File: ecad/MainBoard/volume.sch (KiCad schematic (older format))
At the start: 10 parts, among them Q2 2N4401BU

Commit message: Update BOM and SPIRCE SIM
Add netlist to calculate power dissipation through each resistor
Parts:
- C10: MPN (none) -> CL03A104MP3NNNC
- C11: MPN (none) -> 0603ZD106KAT2A
- C8: Digi-Key_PN (none) -> 1276-1943-2-ND; MPN (none) -> 1276-1943-2-ND
- Q2: MPN 2N4401BU -> 2N4401-ND
- R12: Digi-Key_PN (none) -> 2019-RN73R2ATTD5053F100TR-ND; MPN (none) -> RN73R2ATTD5053F100
- R13, R14: Digi-Key_PN (none) -> RG2012N-474-W-T1; MPN (none) -> RG20N470KWTR-ND
- R15: Digi-Key_PN (none) -> 311-100DGTR-ND; MPN (none) -> RC0100FR-07100RL
- R18: Digi-Key_PN (none) -> A130048TR-ND; MPN (none) -> CRGCQ0402J1K0
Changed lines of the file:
@@
 F 2 "Capacitor_SMD:C_0805_2012Metric_Pad1.18x1.45mm_HandSolder" H 888 650 50  0001 C CNN
 F 3 "~" H 850 800 50  0001 C CNN
+F 4 "1276-1943-2-ND" H 850 800 50  0001 C CNN "Digi-Key_PN"
+F 5 "1276-1943-2-ND" H 850 800 50  0001 C CNN "MPN"
 	1    850  800
 	0    1    1    0
@@
 F 2 "Resistor_SMD:R_0805_2012Metric_Pad1.20x1.40mm_HandSolder" V 1130 800 50  0001 C CNN
 F 3 "~" H 1200 800 50  0001 C CNN
+F 4 "A130048TR-ND" H 1200 800 50  0001 C CNN "Digi-Key_PN"
+F 5 "CRGCQ0402J1K0" H 1200 800 50  0001 C CNN "MPN"
 	1    1200 800
 	0    1    1    0
@@
 F 1 "0u1" V 1739 950 50  0000 C CNN
 F 2 "Capacitor_SMD:C_0805_2012Metric_Pad1.18x1.45mm_HandSolder" H 1938 800 50  0001 C CNN
-F 3 "~" H 1900 950 50  0001 C CNN
+F 3 "http://www.samsungsem.com/kr/support/product-search/mlcc/CL03A104MP3NNNC.jsp" H 1900 950 50  0001 C CNN
 F 4 "C" H 1900 950 50  0001 C CNN "Spice_Primitive"
 F 5 "0.1u" H 1900 950 50  0001 C CNN "Spice_Model"
 F 6 "Y" H 1900 950 50  0001 C CNN "Spice_Netlist_Enabled"
+F 7 "CL03A104MP3NNNC" H 1900 950 50  0001 C CNN "MPN"
 	1    1900 950
 	0    1    1    0
@@
 F 2 "Resistor_SMD:R_0805_2012Metric_Pad1.20x1.40mm_HandSolder" V 2030 1400 50  0001 C CNN
 F 3 "~" H 2100 1400 50  0001 C CNN
+F 4 "2019-RN73R2ATTD5053F100TR-ND" H 2100 1400 50  0001 C CNN "Digi-Key_PN"
+F 5 "RN73R2ATTD5053F100" H 2100 1400 50  0001 C CNN "MPN"
 	1    2100 1400
 	1    0    0    -1
@@
 F 2 "Resistor_SMD:R_0805_2012Metric_Pad1.20x1.40mm_HandSolder" V 2380 1400 50  0001 C CNN
 F 3 "~" H 2450 1400 50  0001 C CNN
+F 4 "RG2012N-474-W-T1" H 2450 1400 50  0001 C CNN "Digi-Key_PN"
+F 5 "RG20N470KWTR-ND" H 2450 1400 50  0001 C CNN "MPN"
 	1    2450 1400
 	1    0    0    -1
@@
 F 1 "100" V 3034 1200 50  0000 C CNN
 F 2 "Resistor_SMD:R_0805_2012Metric_Pad1.20x1.40mm_HandSolder" V 3080 1200 50  0001 C CNN
-F 3 "~" H 3150 1200 50  0001 C CNN
+F 3 "https://www.yageo.com/upload/media/product/productsearch/datasheet/rchip/PYu-RC_Group_51_RoHS_L_11.pdf" H 3150 1200 50  0001 C CNN
+F 4 "311-100DGTR-ND" H 3150 1200 50  0001 C CNN "Digi-Key_PN"
+F 5 "RC0100FR-07100RL" H 3150 1200 50  0001 C CNN "MPN"
 	1    3150 1200
 	0    1    1    0
@@
 F 1 "10u" V 3664 1200 50  0000 C CNN
 F 2 "Capacitor_SMD:C_0805_2012Metric_Pad1.18x1.45mm_HandSolder" H 3538 1050 50  0001 C CNN
-F 3 "~" H 3500 1200 50  0001 C CNN
+F 3 "https://datasheets.avx.com/cx5r.pdf" H 3500 1200 50  0001 C CNN
+F 4 "0603ZD106KAT2A" H 3500 1200 50  0001 C CNN "MPN"
 	1    3500 1200
 	0    -1   -1   0
@@
 F 2 "Resistor_SMD:R_0805_2012Metric_Pad1.20x1.40mm_HandSolder" V 3630 1400 50  0001 C CNN
 F 3 "~" H 3700 1400 50  0001 C CNN
+F 4 "RG2012N-474-W-T1" H 3700 1400 50  0001 C CNN "Digi-Key_PN"
+F 5 "RG20N470KWTR-ND" H 3700 1400 50  0001 C CNN "MPN"
 	1    3700 1400
 	1    0    0    -1
@@
 F 3 "https://www.onsemi.com/pub/Collateral/MMBT4401-D.PDF" H 2550 1250 60  0001 L CNN
 F 4 "2N4401-ND" H 2550 1350 60  0001 L CNN "Digi-Key_PN"
-F 5 "2N4401BU" H 2550 1450 60  0001 L CNN "MPN"
+F 5 "2N4401-ND" H 2550 1450 60  0001 L CNN "MPN"
 F 6 "Discrete Semiconductor Products" H 2550 1550 60  0001 L CNN "Category"
 F 7 "Transistors - Bipolar (BJT) - Single" H 2550 1650 60  0001 L CNN "Family"

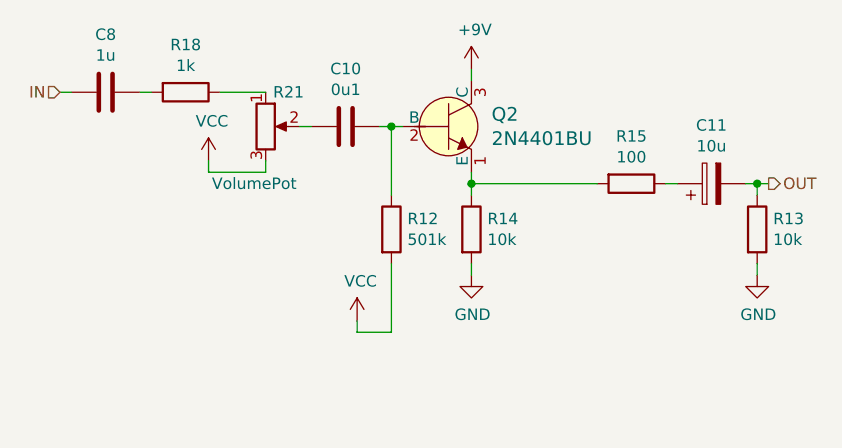
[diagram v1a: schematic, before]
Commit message: Corrections + SPICE Model Finally fixed :)
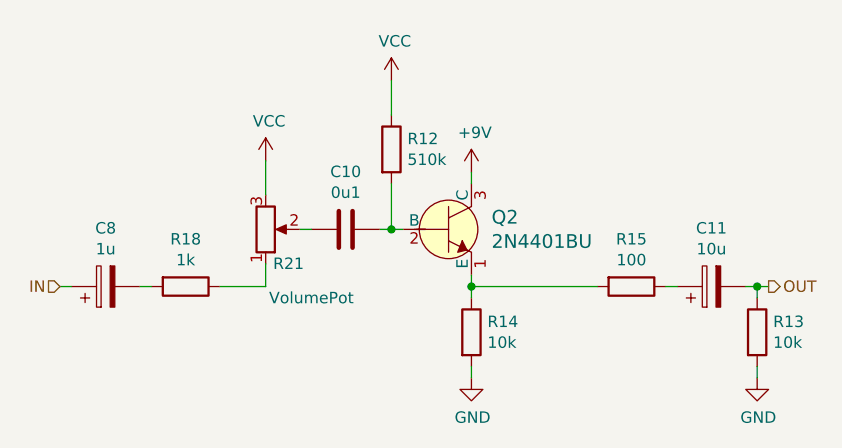
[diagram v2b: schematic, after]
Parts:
- removed C8: 1u, Capacitor_SMD:C_0805_2012Metric_Pad1.18x1.45mm_HandSolder, symbol Device:C
- added C8: 1u, Capacitor_SMD:C_0805_2012Metric_Pad1.18x1.45mm_HandSolder, symbol Device:CP
- Q2: Spice_Lib_File /home/john/dox/cad/screaming-panda/ecad/lib/spice_models/2N4401.lib -> /home/john/dox/cad/screaming-panda/ecad/lib/spice_models/2N4401BU.lib; Spice_Node_Sequence (none) -> 3 2 1
- R12: value 501k -> 510k
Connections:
- net IN: now also C8.1
- net VCC: now also R12.1; no longer R12.2
- net at R18.2: now also C8.2
- net at C10.1, Q2.2 (B): now also R12.2; no longer R12.1
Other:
- moved on the sheet: C10, C11, Q2, R12, R13, R14, R15, R18, R21

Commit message: Clean up ecad
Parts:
- C10: footprint Capacitor_SMD:C_0805_2012Metric_Pad1.18x1.45mm_HandSolder -> Capacitor_SMD:C_0201_0603Metric_Pad0.64x0.40mm_HandSolder; Digi-Key_PN (none) -> 1276-1321-6-ND
- C11: footprint Capacitor_SMD:C_0805_2012Metric_Pad1.18x1.45mm_HandSolder -> Capacitor_SMD:C_0603_1608Metric_Pad1.08x0.95mm_HandSolder; Digi-Key_PN (none) -> 478-10766-6-ND
- C8: footprint Capacitor_SMD:C_0805_2012Metric_Pad1.18x1.45mm_HandSolder -> Capacitor_SMD:C_0603_1608Metric_Pad1.08x0.95mm_HandSolder; Digi-Key_PN (none) -> 0603ZD106KAT2A
- R15: footprint Resistor_SMD:R_0805_2012Metric_Pad1.20x1.40mm_HandSolder -> Resistor_SMD:R_1218_3246Metric_Pad1.22x4.75mm_HandSolder; Digi-Key_PN 311-100DGTR-ND -> 541-100ANDKR-ND; MPN RC0100FR-07100RL -> CRCW1218100RFKEKHP
- R18: footprint Resistor_SMD:R_0805_2012Metric_Pad1.20x1.40mm_HandSolder -> Resistor_SMD:R_0402_1005Metric_Pad0.72x0.64mm_HandSolder
- R21: value VolumePot -> 20ka; Category (none) -> Volume Pot; Digi-Key_PN (none) -> 75160-195-08LF; Spice_Lib_File ../lib/spice_models/pot.lib -> ../lib/spice_models/pots.lib
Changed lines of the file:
@@
 encoding utf-8
 Sheet 4 5
-Title "Effects Board"
-Date "2021-01-17"
-Rev "1.0"
-Comp "Panda Pals"
-Comment1 "John McAvoy"
+Title "Screaming Panda Guitar Pedal"
+Date "2021-08-08"
+Rev "1v0"
+Comp "John McAvoy"
+Comment1 ""
 Comment2 ""
 Comment3 ""
@@
 AR Path="/60332464" Ref="R?"  Part="1"
 AR Path="/6030769F/60332464" Ref="R18"  Part="1"
-F 0 "R18" V 993 1650 50  0000 C CNN
-F 1 "1k" V 1084 1650 50  0000 C CNN
-F 2 "Resistor_SMD:R_0805_2012Metric_Pad1.20x1.40mm_HandSolder" V 1130 1650 50  0001 C CNN
-F 3 "~" H 1200 1650 50  0001 C CNN
+F 0 "R18" V 1100 1650 50  0000 C CNN
+F 1 "1k" V 1200 1650 50  0000 C CNN
+F 2 "Resistor_SMD:R_0402_1005Metric_Pad0.72x0.64mm_HandSolder" V 1130 1650 50  0001 C CNN
+F 3 "https://www.te.com/commerce/DocumentDelivery/DDEController?Action=srchrtrv&DocNm=1773204-3&DocType=DS&DocLang=English" H 1200 1650 50  0001 C CNN
 F 4 "A130048TR-ND" H 1200 1650 50  0001 C CNN "Digi-Key_PN"
 F 5 "CRGCQ0402J1K0" H 1200 1650 50  0001 C CNN "MPN"
@@
 F 0 "C10" V 1648 1400 50  0000 C CNN
 F 1 "0u1" V 1739 1400 50  0000 C CNN
-F 2 "Capacitor_SMD:C_0805_2012Metric_Pad1.18x1.45mm_HandSolder" H 1938 1250 50  0001 C CNN
+F 2 "Capacitor_SMD:C_0201_0603Metric_Pad0.64x0.40mm_HandSolder" H 1938 1250 50  0001 C CNN
 F 3 "http://www.samsungsem.com/kr/support/product-search/mlcc/CL03A104MP3NNNC.jsp" H 1900 1400 50  0001 C CNN
 F 4 "C" H 1900 1400 50  0001 C CNN "Spice_Primitive"
@@
 F 6 "Y" H 1900 1400 50  0001 C CNN "Spice_Netlist_Enabled"
 F 7 "CL03A104MP3NNNC" H 1900 1400 50  0001 C CNN "MPN"
+F 8 "1276-1321-6-ND" H 1900 1400 50  0001 C CNN "Digi-Key_PN"
 	1    1900 1400
 	0    1    1    0
@@
 AR Path="/6030769F/60332476" Ref="R12"  Part="1"
 F 0 "R12" H 2170 1096 50  0000 L CNN
-F 1 "510k" H 2170 1005 50  0000 L CNN
+F 1 "510k" V 2100 950 50  0000 L CNN
 F 2 "Resistor_SMD:R_0805_2012Metric_Pad1.20x1.40mm_HandSolder" V 2030 1050 50  0001 C CNN
-F 3 "~" H 2100 1050 50  0001 C CNN
+F 3 "https://media.digikey.com/pdf/Data%20Sheets/KOA%20Speer/RN73R_Type_DS.pdf" H 2100 1050 50  0001 C CNN
 F 4 "2019-RN73R2ATTD5053F100TR-ND" H 2100 1050 50  0001 C CNN "Digi-Key_PN"
 F 5 "RN73R2ATTD5053F100" H 2100 1050 50  0001 C CNN "MPN"
@@
 AR Path="/6030769F/603324B1" Ref="R14"  Part="1"
 F 0 "R14" H 2520 1896 50  0000 L CNN
-F 1 "10k" H 2520 1805 50  0000 L CNN
+F 1 "10k" V 2450 1750 50  0000 L CNN
 F 2 "Resistor_SMD:R_0805_2012Metric_Pad1.20x1.40mm_HandSolder" V 2380 1850 50  0001 C CNN
-F 3 "~" H 2450 1850 50  0001 C CNN
+F 3 "https://www.susumu.co.jp/common/pdf/n_catalog_partition01_en.pdf" H 2450 1850 50  0001 C CNN
 F 4 "RG2012N-474-W-T1" H 2450 1850 50  0001 C CNN "Digi-Key_PN"
 F 5 "RG20N470KWTR-ND" H 2450 1850 50  0001 C CNN "MPN"
@@
 AR Path="/603324BA" Ref="R?"  Part="1"
 AR Path="/6030769F/603324BA" Ref="R15"  Part="1"
-F 0 "R15" V 2943 1650 50  0000 C CNN
-F 1 "100" V 3034 1650 50  0000 C CNN
-F 2 "Resistor_SMD:R_0805_2012Metric_Pad1.20x1.40mm_HandSolder" V 3080 1650 50  0001 C CNN
-F 3 "https://www.yageo.com/upload/media/product/productsearch/datasheet/rchip/PYu-RC_Group_51_RoHS_L_11.pdf" H 3150 1650 50  0001 C CNN
-F 4 "311-100DGTR-ND" H 3150 1650 50  0001 C CNN "Digi-Key_PN"
-F 5 "RC0100FR-07100RL" H 3150 1650 50  0001 C CNN "MPN"
+F 0 "R15" V 3050 1650 50  0000 C CNN
+F 1 "100" V 3150 1650 50  0000 C CNN
+F 2 "Resistor_SMD:R_1218_3246Metric_Pad1.22x4.75mm_HandSolder" V 3080 1650 50  0001 C CNN
+F 3 "https://www.vishay.com/docs/20043/crcwhpe3.pdf" H 3150 1650 50  0001 C CNN
+F 4 "541-100ANDKR-ND" H 3150 1650 50  0001 C CNN "Digi-Key_PN"
+F 5 "CRCW1218100RFKEKHP" H 3150 1650 50  0001 C CNN "MPN"
 	1    3150 1650
 	0    1    1    0
@@
 F 0 "C11" V 3755 1650 50  0000 C CNN
 F 1 "10u" V 3664 1650 50  0000 C CNN
-F 2 "Capacitor_SMD:C_0805_2012Metric_Pad1.18x1.45mm_HandSolder" H 3538 1500 50  0001 C CNN
+F 2 "Capacitor_SMD:C_0603_1608Metric_Pad1.08x0.95mm_HandSolder" H 3538 1500 50  0001 C CNN
 F 3 "https://datasheets.avx.com/cx5r.pdf" H 3500 1650 50  0001 C CNN
 F 4 "0603ZD106KAT2A" H 3500 1650 50  0001 C CNN "MPN"
+F 5 "478-10766-6-ND" H 3500 1650 50  0001 C CNN "Digi-Key_PN"
 	1    3500 1650
 	0    -1   -1   0
@@
 AR Path="/6030769F/603324C6" Ref="R13"  Part="1"
 F 0 "R13" H 3770 1896 50  0000 L CNN
-F 1 "10k" H 3770 1805 50  0000 L CNN
+F 1 "10k" V 3700 1775 50  0000 L CNN
 F 2 "Resistor_SMD:R_0805_2012Metric_Pad1.20x1.40mm_HandSolder" V 3630 1850 50  0001 C CNN
-F 3 "~" H 3700 1850 50  0001 C CNN
+F 3 "https://www.susumu.co.jp/common/pdf/n_catalog_partition01_en.pdf" H 3700 1850 50  0001 C CNN
 F 4 "RG2012N-474-W-T1" H 3700 1850 50  0001 C CNN "Digi-Key_PN"
 F 5 "RG20N470KWTR-ND" H 3700 1850 50  0001 C CNN "MPN"
@@
 F 0 "C8" V 1105 1650 50  0000 C CNN
 F 1 "1u" V 1014 1650 50  0000 C CNN
-F 2 "Capacitor_SMD:C_0805_2012Metric_Pad1.18x1.45mm_HandSolder" H 888 1500 50  0001 C CNN
+F 2 "Capacitor_SMD:C_0603_1608Metric_Pad1.08x0.95mm_HandSolder" H 888 1500 50  0001 C CNN
 F 3 "https://datasheets.avx.com/cx5r.pdf" H 850 1650 50  0001 C CNN
 F 4 "0603ZD106KAT2A" H 850 1650 50  0001 C CNN "MPN"
+F 5 "0603ZD106KAT2A" H 850 1650 50  0001 C CNN "Digi-Key_PN"
 	1    850  1650
 	0    -1   -1   0
@@
 P 1550 1400
 F 0 "R21" H 1650 1550 50  0000 C CNN
-F 1 "VolumePot" H 1750 1700 50  0000 C CNN
+F 1 "20ka" V 1550 1400 50  0000 C CNN
 F 2 "Connector_PinHeader_2.54mm:PinHeader_1x03_P2.54mm_Vertical" H 1550 1400 50  0001 C CNN
-F 3 "~" H 1550 1400 50  0001 C CNN
+F 3 "https://www.bourns.com/docs/Product-Datasheets/PTV09.pdf" H 1550 1400 50  0001 C CNN
 F 4 "X" H 1550 1400 50  0001 C CNN "Spice_Primitive"
 F 5 "POTVolume" H 1550 1400 50  0001 C CNN "Spice_Model"
 F 6 "Y" H 1550 1400 50  0001 C CNN "Spice_Netlist_Enabled"
-F 7 "../lib/spice_models/pot.lib" H 1550 1400 50  0001 C CNN "Spice_Lib_File"
+F 7 "../lib/spice_models/pots.lib" H 1550 1400 50  0001 C CNN "Spice_Lib_File"
+F 8 "Volume Pot" H 1800 1650 50  0000 C CNN "Category"
+F 9 "75160-195-08LF" H 1550 1400 50  0001 C CNN "Digi-Key_PN"
+F 10 "" H 1550 1400 50  0001 C CNN "MPN"
 	1    1550 1400
 	1    0    0    1

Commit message: Update ecad BOM
Change transistor to 2N4424
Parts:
- C10: value 0u1 -> 100n; footprint Capacitor_SMD:C_0201_0603Metric_Pad0.64x0.40mm_HandSolder -> Capacitor_SMD:C_0805_2012Metric_Pad1.18x1.45mm_HandSolder; MPN CL03A104MP3NNNC -> C0805C104K3RACTU
- C11: footprint Capacitor_SMD:C_0603_1608Metric_Pad1.08x0.95mm_HandSolder -> Capacitor_SMD:C_0805_2012Metric_Pad1.18x1.45mm_HandSolder; MPN 0603ZD106KAT2A -> C0805C106K8PACTU
- C8: footprint Capacitor_SMD:C_0603_1608Metric_Pad1.08x0.95mm_HandSolder -> Capacitor_SMD:C_0805_2012Metric_Pad1.18x1.45mm_HandSolder; MPN 0603ZD106KAT2A -> C0805C105K4RACTU
- Q2: value 2N4401BU -> 2N4424; MPN 2N4401-ND -> 2N4424; Spice_Lib_File /home/john/dox/cad/screaming-panda/ecad/lib/spice_models/2N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 -> ../lib/spice_models/2N4424.lib; Spice_Model 2N4401 -> 2N4424
- R12: MPN RN73R2ATTD5053F100 -> ERJ-6ENF5103V
- R13, R14: MPN RG20N470KWTR-ND -> ERJ-6GEYJ103V
- R15: footprint Resistor_SMD:R_1218_3246Metric_Pad1.22x4.75mm_HandSolder -> Resistor_SMD:R_0805_2012Metric_Pad1.20x1.40mm_HandSolder; MPN CRCW1218100RFKEKHP -> ERJ-6GEYJ101V
- R18: footprint Resistor_SMD:R_0402_1005Metric_Pad0.72x0.64mm_HandSolder -> Resistor_SMD:R_0805_2012Metric_Pad1.20x1.40mm_HandSolder; MPN CRGCQ0402J1K0 -> ERA6AEB102V
- R21: footprint Connector_PinHeader_2.54mm:PinHeader_1x03_P2.54mm_Vertical -> DigiKey:PinHeader_1x3_P2.54_Drill1.1mm; MPN (none) -> 0901200160
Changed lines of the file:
@@
 F 0 "R18" V 1100 1650 50  0000 C CNN
 F 1 "1k" V 1200 1650 50  0000 C CNN
-F 2 "Resistor_SMD:R_0402_1005Metric_Pad0.72x0.64mm_HandSolder" V 1130 1650 50  0001 C CNN
-F 3 "https://www.te.com/commerce/DocumentDelivery/DDEController?Action=srchrtrv&DocNm=1773204-3&DocType=DS&DocLang=English" H 1200 1650 50  0001 C CNN
+F 2 "Resistor_SMD:R_0805_2012Metric_Pad1.20x1.40mm_HandSolder" V 1130 1650 50  0001 C CNN
+F 3 "https://datasheet.octopart.com/ERA6AEB102V-Panasonic-datasheet-62287448.pdf" H 1200 1650 50  0001 C CNN
 F 4 "A130048TR-ND" H 1200 1650 50  0001 C CNN "Digi-Key_PN"
-F 5 "CRGCQ0402J1K0" H 1200 1650 50  0001 C CNN "MPN"
+F 5 "ERA6AEB102V" H 1200 1650 50  0001 C CNN "MPN"
 	1    1200 1650
 	0    1    1    0
@@
 AR Path="/6030769F/60332470" Ref="C10"  Part="1"
 F 0 "C10" V 1648 1400 50  0000 C CNN
-F 1 "0u1" V 1739 1400 50  0000 C CNN
-F 2 "Capacitor_SMD:C_0201_0603Metric_Pad0.64x0.40mm_HandSolder" H 1938 1250 50  0001 C CNN
-F 3 "http://www.samsungsem.com/kr/support/product-search/mlcc/CL03A104MP3NNNC.jsp" H 1900 1400 50  0001 C CNN
+F 1 "100n" V 1739 1400 50  0000 C CNN
+F 2 "Capacitor_SMD:C_0805_2012Metric_Pad1.18x1.45mm_HandSolder" H 1938 1250 50  0001 C CNN
+F 3 "https://datasheet.octopart.com/C0805C104K3RAC-TU-Kemet-datasheet-5313890.pdf" H 1900 1400 50  0001 C CNN
 F 4 "C" H 1900 1400 50  0001 C CNN "Spice_Primitive"
 F 5 "0.1u" H 1900 1400 50  0001 C CNN "Spice_Model"
 F 6 "Y" H 1900 1400 50  0001 C CNN "Spice_Netlist_Enabled"
-F 7 "CL03A104MP3NNNC" H 1900 1400 50  0001 C CNN "MPN"
+F 7 "C0805C104K3RACTU" H 1900 1400 50  0001 C CNN "MPN"
 F 8 "1276-1321-6-ND" H 1900 1400 50  0001 C CNN "Digi-Key_PN"
 	1    1900 1400
@@
 F 1 "510k" V 2100 950 50  0000 L CNN
 F 2 "Resistor_SMD:R_0805_2012Metric_Pad1.20x1.40mm_HandSolder" V 2030 1050 50  0001 C CNN
-F 3 "https://media.digikey.com/pdf/Data%20Sheets/KOA%20Speer/RN73R_Type_DS.pdf" H 2100 1050 50  0001 C CNN
+F 3 "https://datasheet.octopart.com/ERJ-6ENF5103V-Panasonic-datasheet-13266541.pdf" H 2100 1050 50  0001 C CNN
 F 4 "2019-RN73R2ATTD5053F100TR-ND" H 2100 1050 50  0001 C CNN "Digi-Key_PN"
-F 5 "RN73R2ATTD5053F100" H 2100 1050 50  0001 C CNN "MPN"
+F 5 "ERJ-6ENF5103V" H 2100 1050 50  0001 C CNN "MPN"
 	1    2100 1050
 	1    0    0    -1
@@
 F 1 "10k" V 2450 1750 50  0000 L CNN
 F 2 "Resistor_SMD:R_0805_2012Metric_Pad1.20x1.40mm_HandSolder" V 2380 1850 50  0001 C CNN
-F 3 "https://www.susumu.co.jp/common/pdf/n_catalog_partition01_en.pdf" H 2450 1850 50  0001 C CNN
+F 3 "https://datasheet.octopart.com/ERJ-6GEYJ103V-Panasonic-datasheet-13266872.pdf" H 2450 1850 50  0001 C CNN
 F 4 "RG2012N-474-W-T1" H 2450 1850 50  0001 C CNN "Digi-Key_PN"
-F 5 "RG20N470KWTR-ND" H 2450 1850 50  0001 C CNN "MPN"
+F 5 "ERJ-6GEYJ103V" H 2450 1850 50  0001 C CNN "MPN"
 	1    2450 1850
 	1    0    0    -1
@@
 F 0 "R15" V 3050 1650 50  0000 C CNN
 F 1 "100" V 3150 1650 50  0000 C CNN
-F 2 "Resistor_SMD:R_1218_3246Metric_Pad1.22x4.75mm_HandSolder" V 3080 1650 50  0001 C CNN
-F 3 "https://www.vishay.com/docs/20043/crcwhpe3.pdf" H 3150 1650 50  0001 C CNN
+F 2 "Resistor_SMD:R_0805_2012Metric_Pad1.20x1.40mm_HandSolder" V 3080 1650 50  0001 C CNN
+F 3 "https://datasheet.octopart.com/ERJ-6GEYJ101V-Panasonic-datasheet-13266872.pdf" H 3150 1650 50  0001 C CNN
 F 4 "541-100ANDKR-ND" H 3150 1650 50  0001 C CNN "Digi-Key_PN"
-F 5 "CRCW1218100RFKEKHP" H 3150 1650 50  0001 C CNN "MPN"
+F 5 "ERJ-6GEYJ101V" H 3150 1650 50  0001 C CNN "MPN"
 	1    3150 1650
 	0    1    1    0
@@
 F 0 "C11" V 3755 1650 50  0000 C CNN
 F 1 "10u" V 3664 1650 50  0000 C CNN
-F 2 "Capacitor_SMD:C_0603_1608Metric_Pad1.08x0.95mm_HandSolder" H 3538 1500 50  0001 C CNN
-F 3 "https://datasheets.avx.com/cx5r.pdf" H 3500 1650 50  0001 C CNN
-F 4 "0603ZD106KAT2A" H 3500 1650 50  0001 C CNN "MPN"
+F 2 "Capacitor_SMD:C_0805_2012Metric_Pad1.18x1.45mm_HandSolder" H 3538 1500 50  0001 C CNN
+F 3 "https://datasheet.octopart.com/C0805C106K8PACTU-KEMET-datasheet-149523945.pdf" H 3500 1650 50  0001 C CNN
+F 4 "C0805C106K8PACTU" H 3500 1650 50  0001 C CNN "MPN"
 F 5 "478-10766-6-ND" H 3500 1650 50  0001 C CNN "Digi-Key_PN"
 	1    3500 1650
@@
 F 1 "10k" V 3700 1775 50  0000 L CNN
 F 2 "Resistor_SMD:R_0805_2012Metric_Pad1.20x1.40mm_HandSolder" V 3630 1850 50  0001 C CNN
-F 3 "https://www.susumu.co.jp/common/pdf/n_catalog_partition01_en.pdf" H 3700 1850 50  0001 C CNN
+F 3 "https://datasheet.octopart.com/ERJ-6GEYJ103V-Panasonic-datasheet-13266872.pdf" H 3700 1850 50  0001 C CNN
 F 4 "RG2012N-474-W-T1" H 3700 1850 50  0001 C CNN "Digi-Key_PN"
-F 5 "RG20N470KWTR-ND" H 3700 1850 50  0001 C CNN "MPN"
+F 5 "ERJ-6GEYJ103V" H 3700 1850 50  0001 C CNN "MPN"
 	1    3700 1850
 	1    0    0    -1
@@
 F 0 "C8" V 1105 1650 50  0000 C CNN
 F 1 "1u" V 1014 1650 50  0000 C CNN
-F 2 "Capacitor_SMD:C_0603_1608Metric_Pad1.08x0.95mm_HandSolder" H 888 1500 50  0001 C CNN
-F 3 "https://datasheets.avx.com/cx5r.pdf" H 850 1650 50  0001 C CNN
-F 4 "0603ZD106KAT2A" H 850 1650 50  0001 C CNN "MPN"
+F 2 "Capacitor_SMD:C_0805_2012Metric_Pad1.18x1.45mm_HandSolder" H 888 1500 50  0001 C CNN
+F 3 "https://datasheet.octopart.com/C0805C105K4RACTU-KEMET-datasheet-149523919.pdf" H 850 1650 50  0001 C CNN
+F 4 "C0805C105K4RACTU" H 850 1650 50  0001 C CNN "MPN"
 F 5 "0603ZD106KAT2A" H 850 1650 50  0001 C CNN "Digi-Key_PN"
 	1    850  1650
@@
 AR Path="/6030769F/60332485" Ref="Q2"  Part="1"
 F 0 "Q2" H 2538 1453 60  0000 L CNN
-F 1 "2N4401BU" H 2538 1347 60  0000 L CNN
+F 1 "2N4424" H 2538 1347 60  0000 L CNN
 F 2 "digikey-footprints:TO-92-3" H 2550 1600 60  0001 L CNN
-F 3 "https://www.onsemi.com/pub/Collateral/MMBT4401-D.PDF" H 2550 1700 60  0001 L CNN
+F 3 "" H 2550 1700 60  0001 L CNN
 F 4 "2N4401-ND" H 2550 1800 60  0001 L CNN "Digi-Key_PN"
-F 5 "2N4401-ND" H 2550 1900 60  0001 L CNN "MPN"
+F 5 "2N4424" H 2550 1900 60  0001 L CNN "MPN"
 F 6 "Discrete Semiconductor Products" H 2550 2000 60  0001 L CNN "Category"
 F 7 "Transistors - Bipolar (BJT) - Single" H 2550 2100 60  0001 L CNN "Family"
@@
 F 11 "ON Semiconductor" H 2550 2500 60  0001 L CNN "Manufacturer"
 F 12 "Active" H 2550 2600 60  0001 L CNN "Status"
-F 13 "/home/john/dox/cad/screaming-panda/ecad/lib/spice_models/2N4401BU.lib" H 2350 1400 50  0001 C CNN "Spice_Lib_File"
-F 14 "2N4401" H 2350 1400 50  0001 C CNN "Spice_Model"
+F 13 "../lib/spice_models/2N4424.lib" H 2350 1400 50  0001 C CNN "Spice_Lib_File"
+F 14 "2N4424" H 2350 1400 50  0001 C CNN "Spice_Model"
 F 15 "Y" H 2350 1400 50  0001 C CNN "Spice_Netlist_Enabled"
 F 16 "Q" H 2350 1400 50  0001 C CNN "Spice_Primitive"
@@
 F 0 "R21" H 1650 1550 50  0000 C CNN
 F 1 "20ka" V 1550 1400 50  0000 C CNN
-F 2 "Connector_PinHeader_2.54mm:PinHeader_1x03_P2.54mm_Vertical" H 1550 1400 50  0001 C CNN
-F 3 "https://www.bourns.com/docs/Product-Datasheets/PTV09.pdf" H 1550 1400 50  0001 C CNN
+F 2 "DigiKey:PinHeader_1x3_P2.54_Drill1.1mm" H 1550 1400 50  0001 C CNN
+F 3 "https://www.molex.com/pdm_docs/sd/901200160_sd.pdf" H 1550 1400 50  0001 C CNN
 F 4 "X" H 1550 1400 50  0001 C CNN "Spice_Primitive"
 F 5 "POTVolume" H 1550 1400 50  0001 C CNN "Spice_Model"
@@
 F 8 "Volume Pot" H 1800 1650 50  0000 C CNN "Category"
 F 9 "75160-195-08LF" H 1550 1400 50  0001 C CNN "Digi-Key_PN"
-F 10 "" H 1550 1400 50  0001 C CNN "MPN"
+F 10 "0901200160" H 1550 1400 50  0001 C CNN "MPN"
 	1    1550 1400
 	1    0    0    1

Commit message: Library recovery
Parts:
- Q2: footprint digikey-footprints:TO-92-3 -> screaming-panda:TO-92-3_Formed_Leads
- R21: footprint DigiKey:PinHeader_1x3_P2.54_Drill1.1mm -> screaming-panda:75160-195-03LF
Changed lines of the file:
@@
 F 0 "Q2" H 2538 1453 60  0000 L CNN
 F 1 "2N4424" H 2538 1347 60  0000 L CNN
-F 2 "digikey-footprints:TO-92-3" H 2550 1600 60  0001 L CNN
-F 3 "" H 2550 1700 60  0001 L CNN
+F 2 "screaming-panda:TO-92-3_Formed_Leads" H 2550 1600 60  0001 L CNN
+F 3 "https://my.centralsemi.com/datasheets/2N4424.PDF" H 2550 1700 60  0001 L CNN
 F 4 "2N4401-ND" H 2550 1800 60  0001 L CNN "Digi-Key_PN"
 F 5 "2N4424" H 2550 1900 60  0001 L CNN "MPN"
@@
 F 0 "R21" H 1650 1550 50  0000 C CNN
 F 1 "20ka" V 1550 1400 50  0000 C CNN
-F 2 "DigiKey:PinHeader_1x3_P2.54_Drill1.1mm" H 1550 1400 50  0001 C CNN
+F 2 "screaming-panda:75160-195-03LF" H 1550 1400 50  0001 C CNN
 F 3 "https://www.molex.com/pdm_docs/sd/901200160_sd.pdf" H 1550 1400 50  0001 C CNN
 F 4 "X" H 1550 1400 50  0001 C CNN "Spice_Primitive"
